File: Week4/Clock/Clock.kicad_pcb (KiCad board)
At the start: 2 copper layers, 140 x 90 mm, 41 parts, among them J1 PJ-102AH, J2 Conn_01x06, SW1 RotaryEncoder_Switch, SW2 Omron_B3F_SPST, U1 WH2004A-CFH-JT#, U2 ATmega328-PU, U3 L7805_TO92, U4 DS1307_DIP-8, U5 MAX7219, U6 MAX7219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

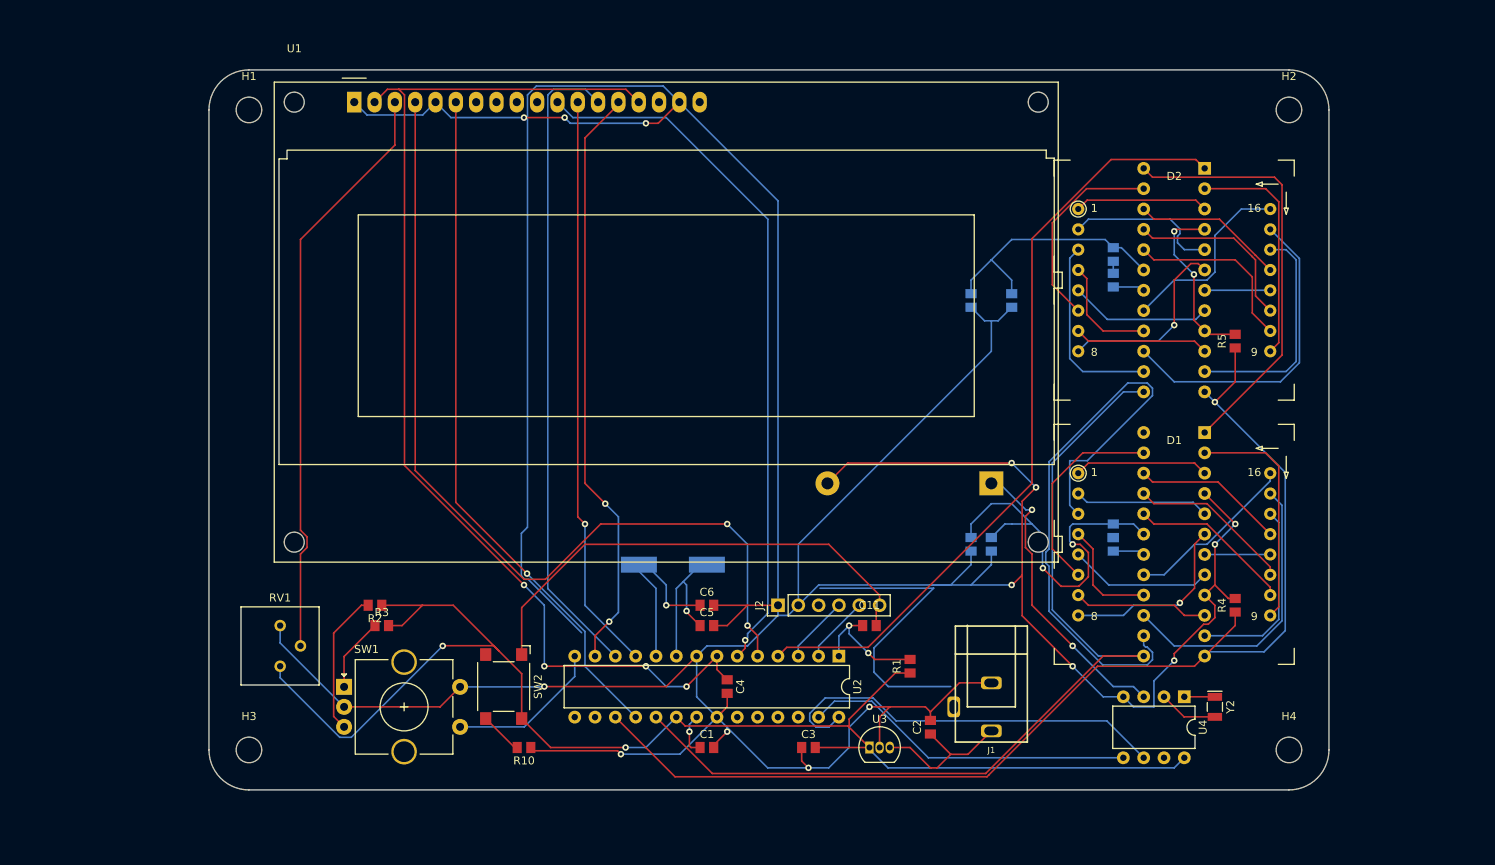
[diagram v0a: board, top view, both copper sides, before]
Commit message: Updated Schema & PCB
PCB was completely redone with only two DRC warnings which pertain to the Power In but nothing big, Changed to smaller LCD (Thankfully more space)
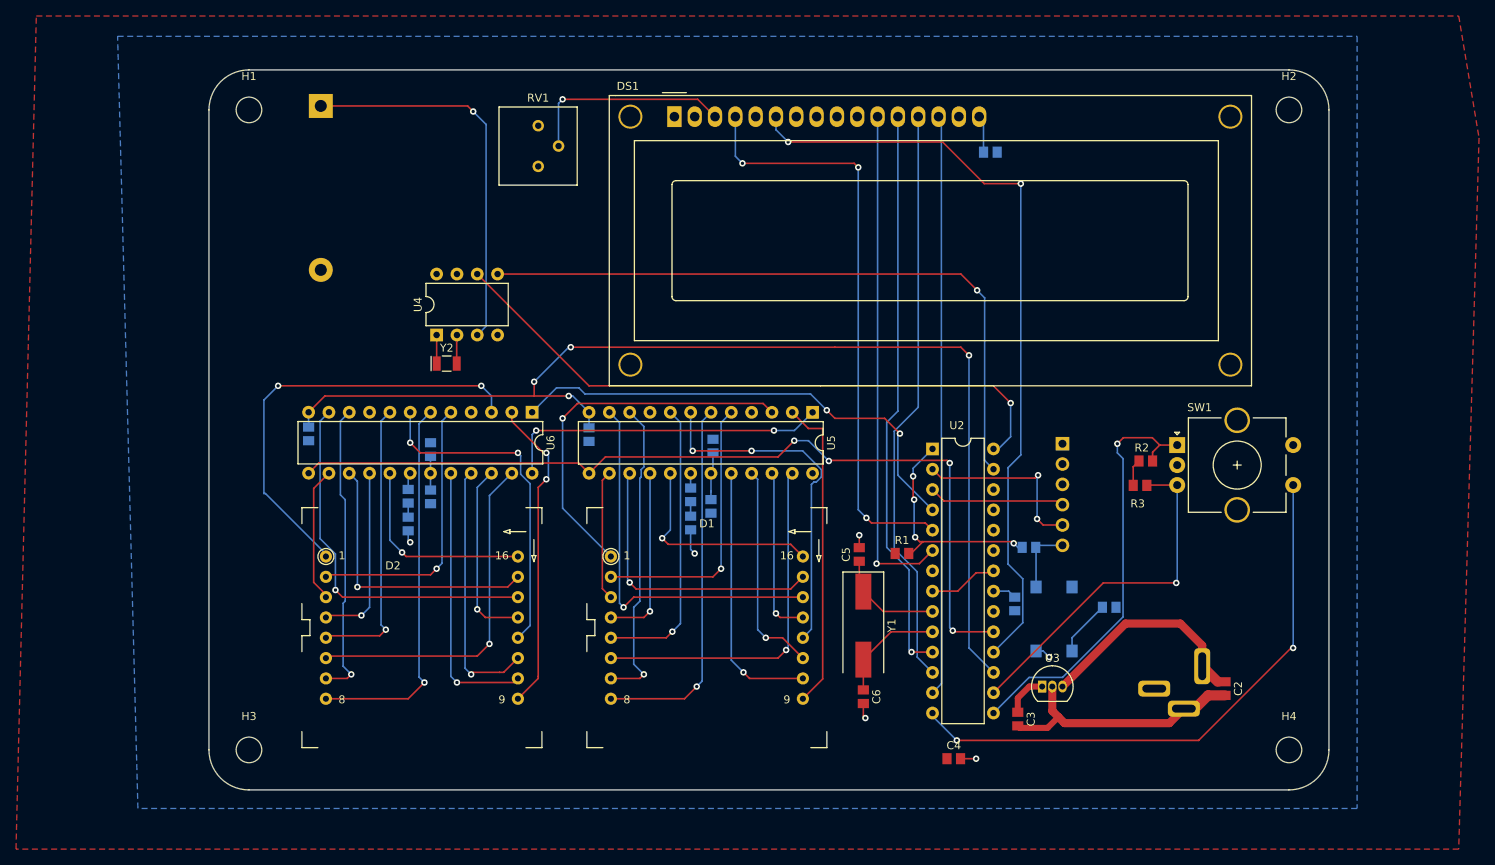
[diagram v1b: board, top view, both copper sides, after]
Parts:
- removed U1: WH2004A-CFH-JT#, footprints:WH2004A-CFH-JT#
- added DS1: TC1602A-01T, footprints:TC1602A-01T, F.Cu at (138.2, 60.8)
- added R11: R_0805_1K, footprints:R_0805_2012Metric, B.Cu at (177.7, 65.3)
- C1, C11, J2, R10, R4, R5, SW2: moved to B.Cu
- J1: value PJ-102AH -> Power_inlet_vertical; footprint footprints:PJ-102AH -> footprints:Wurth-694106402002; moved to B.Cu
- SW1: footprint footprints:RotaryEncoder_Alps_EC11E-Switch_Vertical_H20mm_CircularMountingHoles -> footprints:RotaryEncoder_TT_EN11-Switch_Vertical_H20mm_CircularMountingHoles
- U5, U6, Y1: moved to F.Cu
- moved R5 116.4 mm to (92.5, 100.5), turned to -90 degrees
- moved SW1 108.4 mm to (201.0, 101.9)
- moved Y2 105.2 mm to (109.7, 91.7), turned to 0 degrees
- moved U4 103.8 mm to (108.5, 88.1), turned to 90 degrees
- moved D2 103.6 mm to (106.6, 124.7)
- moved R3 97.7 mm to (197.1, 103.9), turned to 180 degrees
- moved R2 96.8 mm to (196.4, 106.9), turned to 0 degrees
- moved BT1 96.2 mm to (94.0, 59.5), turned to -90 degrees
- moved R8 94.4 mm to (104.9, 111.8), turned to 90 degrees
- moved R9 92.2 mm to (104.9, 108.3), turned to 90 degrees
- moved U6 89.4 mm to (120.4, 97.8), turned to -90 degrees
- moved R4 83.5 mm to (127.5, 100.6), turned to -90 degrees
- moved R10 75.2 mm to (192.5, 122.2)
- moved C10 75.0 mm to (107.7, 102.5), turned to 90 degrees
- moved C8 71.9 mm to (107.7, 108.4)
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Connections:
- C10 pad 1: Net-(C10-Pad1) -> VCC
- C7 pad 1: Net-(C7-Pad1) -> VCC
- C8 pad 1: Net-(C10-Pad1) -> VCC
- C9 pad 1: Net-(C7-Pad1) -> VCC
- R2 pad 2: Net-(R2-Pad2) -> ROT ENC B OUT
- R3 pad 1: Net-(R3-Pad1) -> ROT ENC A OUT
- R6 pad 1: Net-(C7-Pad1) -> VCC
- R8 pad 1: Net-(C10-Pad1) -> VCC
- SW1 pad A: Net-(R3-Pad1) -> ROT ENC A OUT
- SW1 pad B: Net-(R2-Pad2) -> ROT ENC B OUT
- U5 pad 19: Net-(C7-Pad1) -> VCC
- U6 pad 19: Net-(C10-Pad1) -> VCC
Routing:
- net GND: track 607.4 -> 46.6 mm, vias 17 -> 3
- net VCC: track 317.4 -> 25.6 mm, vias 6 -> 3
- net Net-(D1-Pad3): track 77.6 -> 16.3 mm
- net ROT ENC A OUT: track 0.00 -> 53.6 mm, vias 0 -> 1
- net ROT ENC SWITCH: track 19.5 -> 71.9 mm, vias 0 -> 2
- net ~{RESET BTN}: track 60.5 -> 8.42 mm
- net Net-(C7-Pad1): track 48.4 -> 0.00 mm, vias 2 -> 0
- net Net-(DS1-Pad3): track 73.5 -> 26.0 mm, vias 0 -> 1
- net ROT ENC B OUT: track 0.00 -> 44.6 mm, vias 0 -> 1
- net A4 SDA: track 41.9 -> 84.0 mm, vias 0 -> 1
- net (no net): track 38.1 -> 0.00 mm
- net Net-(D2-Pad1): track 16.7 -> 54.4 mm, vias 0 -> 2
- net LCD RS: track 111.6 -> 74.0 mm, vias 2 -> 3
- net LOAD MAX: track 97.4 -> 61.0 mm, vias 0 -> 2
- net Net-(D1-Pad12): track 8.20 -> 44.1 mm, vias 0 -> 2
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- added copper zone on B.Cu, net GND
- added copper zone on F.Cu, net VCC

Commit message: Fixed major DRC issues
Only DRC issues now are due to my logo :(
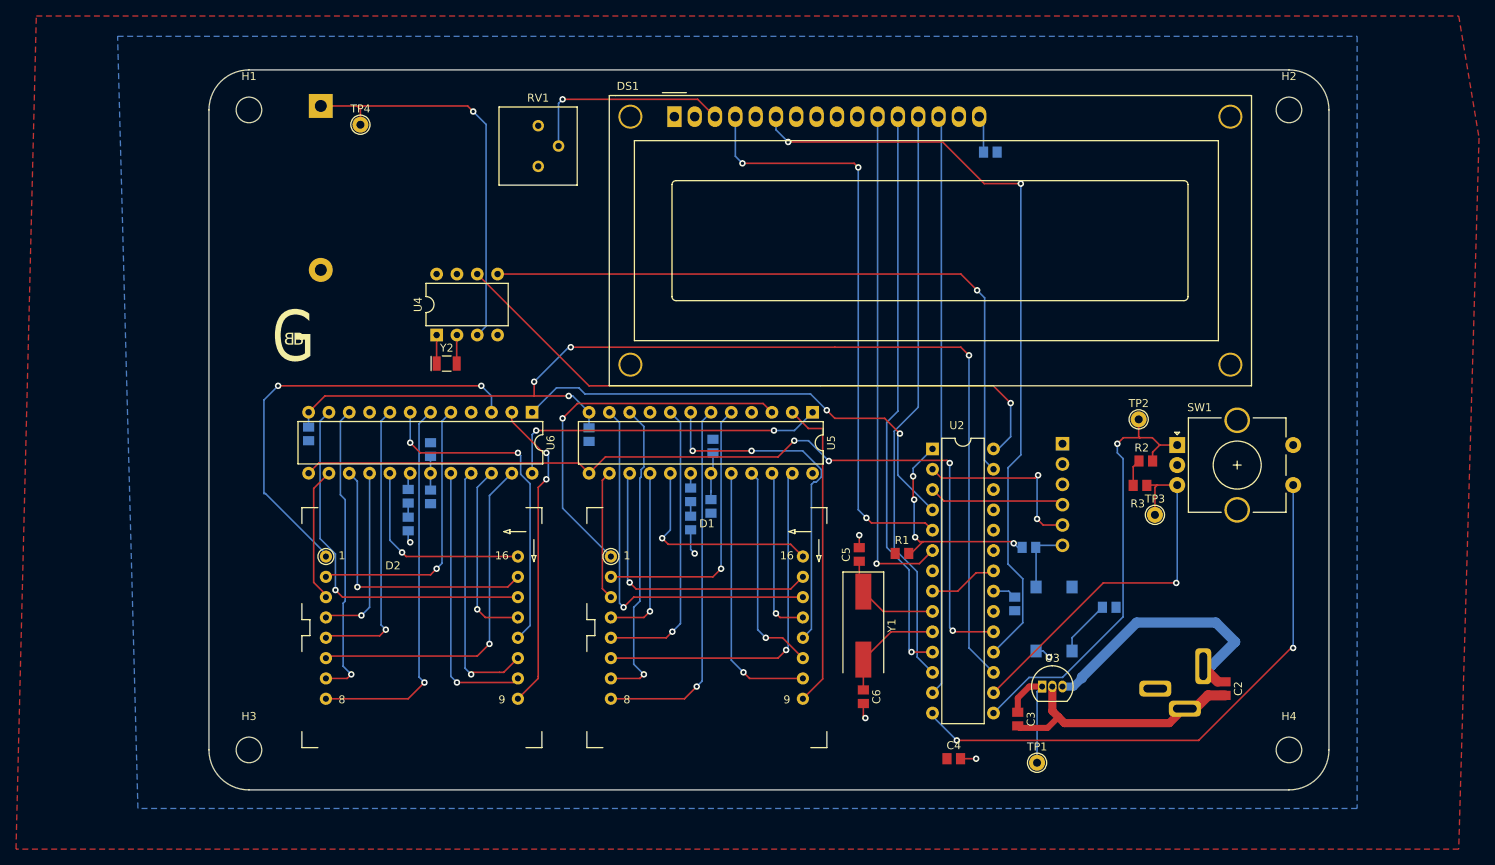
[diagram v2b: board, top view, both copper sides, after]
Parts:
- added TP1: TestPoint, footprints:TestPoint_THTPad_D2.0mm_Drill1.0mm, F.Cu at (183.5, 141.6)
- added TP2: TestPoint, footprints:TestPoint_THTPad_D2.0mm_Drill1.0mm, F.Cu at (196.2, 98.7)
- added TP3: TestPoint, footprints:TestPoint_THTPad_D2.0mm_Drill1.0mm, F.Cu at (198.2, 110.6)
- added TP4: TestPoint, footprints:TestPoint_THTPad_D2.0mm_Drill1.0mm, F.Cu at (98.9, 61.8)
- moved J1 0.13 mm to (200.8, 129.5)
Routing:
- net VCC: track 25.6 -> 35.4 mm
- net Net-(C2-Pad1): track 28.1 -> 34.9 mm
- net ROT ENC B OUT: track 44.6 -> 48.5 mm
- net VBAT: track 48.4 -> 50.9 mm
- net ROT ENC A OUT: track 53.6 -> 56.0 mm
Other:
- board text added: "B"
- board text added: "G"

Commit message: Fixed ALL DRC Warnings
Mark the works of this Github Commit, this clock PCB will be amazing (Added proper logo to PCB and Schema)
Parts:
- added G***: LOGO, Logo:Logo, B.Cu at (195.4, 79.2)
- moved TP4 3.32 mm to (102.2, 61.5)
- moved TP3 0.38 mm to (197.9, 110.6)
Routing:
- net VBAT: track 50.9 -> 53.0 mm
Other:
- board text removed: "B"
- board text removed: "G"

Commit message: Added Fetus Arduino Code
Baby Clock Code has been added
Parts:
- added G***: LOGO, footprints:HPS_logo, B.Cu at (140.8, 72.9)
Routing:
- net Net-(D1-Pad14): track 48.0 -> 46.1 mm
- net Net-(D2-Pad8): track 47.8 -> 46.7 mm
- net VCC: track 35.4 -> 36.4 mm
- net Net-(D2-Pad5): track 35.6 -> 34.7 mm
- net LCD E: track 96.5 -> 95.7 mm
- net Net-(D2-Pad6): track 43.5 -> 44.1 mm

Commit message: Fixed Clock code and added copperto logo
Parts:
- moved G*** 0.52 mm to (195.2, 78.7)
